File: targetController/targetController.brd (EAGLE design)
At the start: 63.2 x 83.8 mm, 52 parts, among them Q1 MOSFET-NCHANNELBSS123LT1G, Q10 2n3904, Q11 MOSFET-NCHANNELBSS123LT1G, Q12 2n3904, Q13 MOSFET-NCHANNELBSS123LT1G, Q14 2n3904, Q15 MOSFET-NCHANNELBSS123LT1G, Q16 2n3904, Q17 MOSFET-NCHANNELBSS123LT1G, Q18 2n3904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

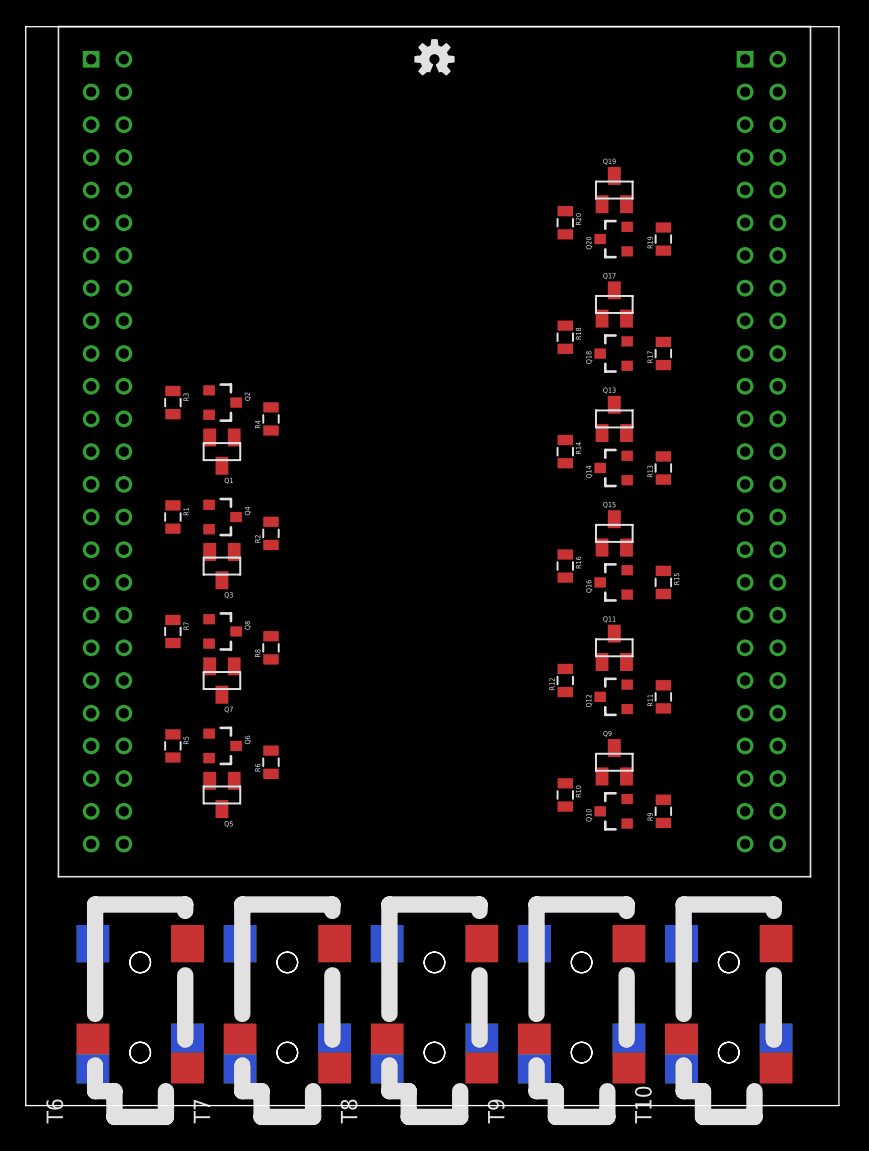
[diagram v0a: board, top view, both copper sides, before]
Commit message: Routed targetController
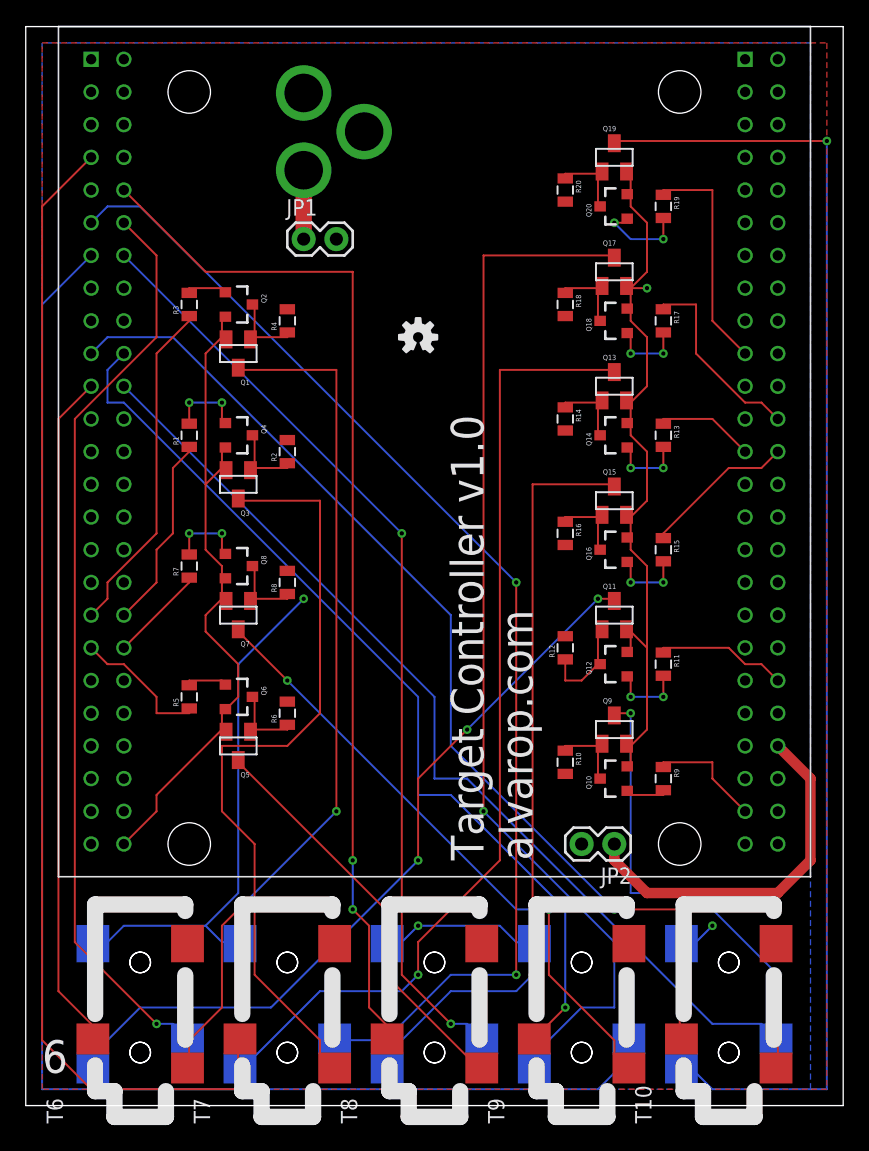
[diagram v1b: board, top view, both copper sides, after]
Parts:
- added J1: POWER_JACKPTH, SparkFun-Connectors:POWER_JACK_PTH
- added JP1, JP2: M02PTH, SparkFun-Connectors:1X02
- added U$2, U$3, U$4, U$5: (no value), SparkFun-Electromechanical:STAND-OFF
- moved LOGO1 21.6 mm to (30.5, 59.7)
- moved Q1 7.73 mm to (16.5, 58.4)
- moved Q2 7.73 mm to (16.5, 62.2)
- moved R3 7.73 mm to (12.7, 62.2), turned to 90 degrees
- moved R4 7.73 mm to (20.3, 61.0)
- moved Q3 6.48 mm to (16.5, 48.3)
- moved Q4 6.48 mm to (16.5, 52.1)
- moved R1 6.48 mm to (12.7, 52.1), turned to 90 degrees
- moved R2 6.48 mm to (20.3, 50.8)
- moved Q7 5.24 mm to (16.5, 38.1)
- moved Q8 5.24 mm to (16.5, 41.9)
- moved R7 5.24 mm to (12.7, 41.9), turned to 90 degrees
- moved R8 5.24 mm to (20.3, 40.6)
- moved Q5 4.02 mm to (16.5, 27.9)
- moved Q6 4.02 mm to (16.5, 31.8)
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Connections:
- new net N$2: J1.PWR, JP1.1
- new net USB_5V: JP2.1, U$1.P$94
- net 5V: now also JP1.2, JP2.2, U$1.P$53, U$1.P$54
- net GND: now also J1.GND, U$1.P$1, U$1.P$100, U$1.P$2, U$1.P$49, U$1.P$50, U$1.P$51, U$1.P$52, U$1.P$99
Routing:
- net VSENSE4: track 0.00 -> 114.6 mm
- net GND: track 0.00 -> 112.1 mm, vias 0 -> 1
- net TGTGND5: track 0.00 -> 102.2 mm, vias 0 -> 1
- net VSENSE2: track 0.00 -> 92.4 mm, vias 0 -> 2
- net VSENSE7: track 0.00 -> 91.0 mm
- net TGTGND4: track 0.00 -> 81.8 mm, vias 0 -> 1
- net VSENSE8: track 0.00 -> 81.1 mm, vias 0 -> 2
- net VSENSE10: track 0.00 -> 80.7 mm, vias 0 -> 1
- net TGTGND2: track 0.00 -> 75.5 mm, vias 0 -> 1
- net VSENSE5: track 0.00 -> 75.4 mm
- net VSENSE3: track 0.00 -> 73.1 mm, vias 0 -> 2
- net VSENSE9: track 0.00 -> 71.7 mm, vias 0 -> 1
- net VSENSE1: track 0.00 -> 71.4 mm, vias 0 -> 1
- net TGTGND6: track 0.00 -> 66.8 mm, vias 0 -> 2
- net TGTGND7: track 0.00 -> 60.4 mm
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- added copper zone on layer 1, net 5V
- added copper zone on layer 16, net GND
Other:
- board size 63.2 x 83.8 mm -> 63.5 x 83.8 mm
- board text added: "1"
- board text added: "6"
- board text added: "Target Controller v1.0"
- board text added: "alvarop.com"
